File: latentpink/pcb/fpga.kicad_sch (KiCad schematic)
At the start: 0 parts

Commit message: Continued initial schematic capture and floorplanning
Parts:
- added J1: CONN_SFP_HOST, azonenberg_pcb:CONN_SFP+_AMPHENOL_UE76_A10_2000T, symbol special-azonenberg:CONN_SFP_HOST
- added J2: SFP_CAGE, azonenberg_pcb:CONN_SFP_CAGE_TE_2007194-1, symbol conn:CONN_01X01
- added U2: XC7K160T-2FBG484C, azonenberg_pcb:BGA_484_22x22_FULLARRAY_1MM, symbol xilinx-azonenberg:XC7KxT-FBG484
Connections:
- new net GND: J2.1 (P1)
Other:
- added sheet FPGA Power (fpgapwr.kicad_sch)
- added sheet QDR SRAM (qdr.kicad_sch)
- company: (none) -> Antikernel Labs

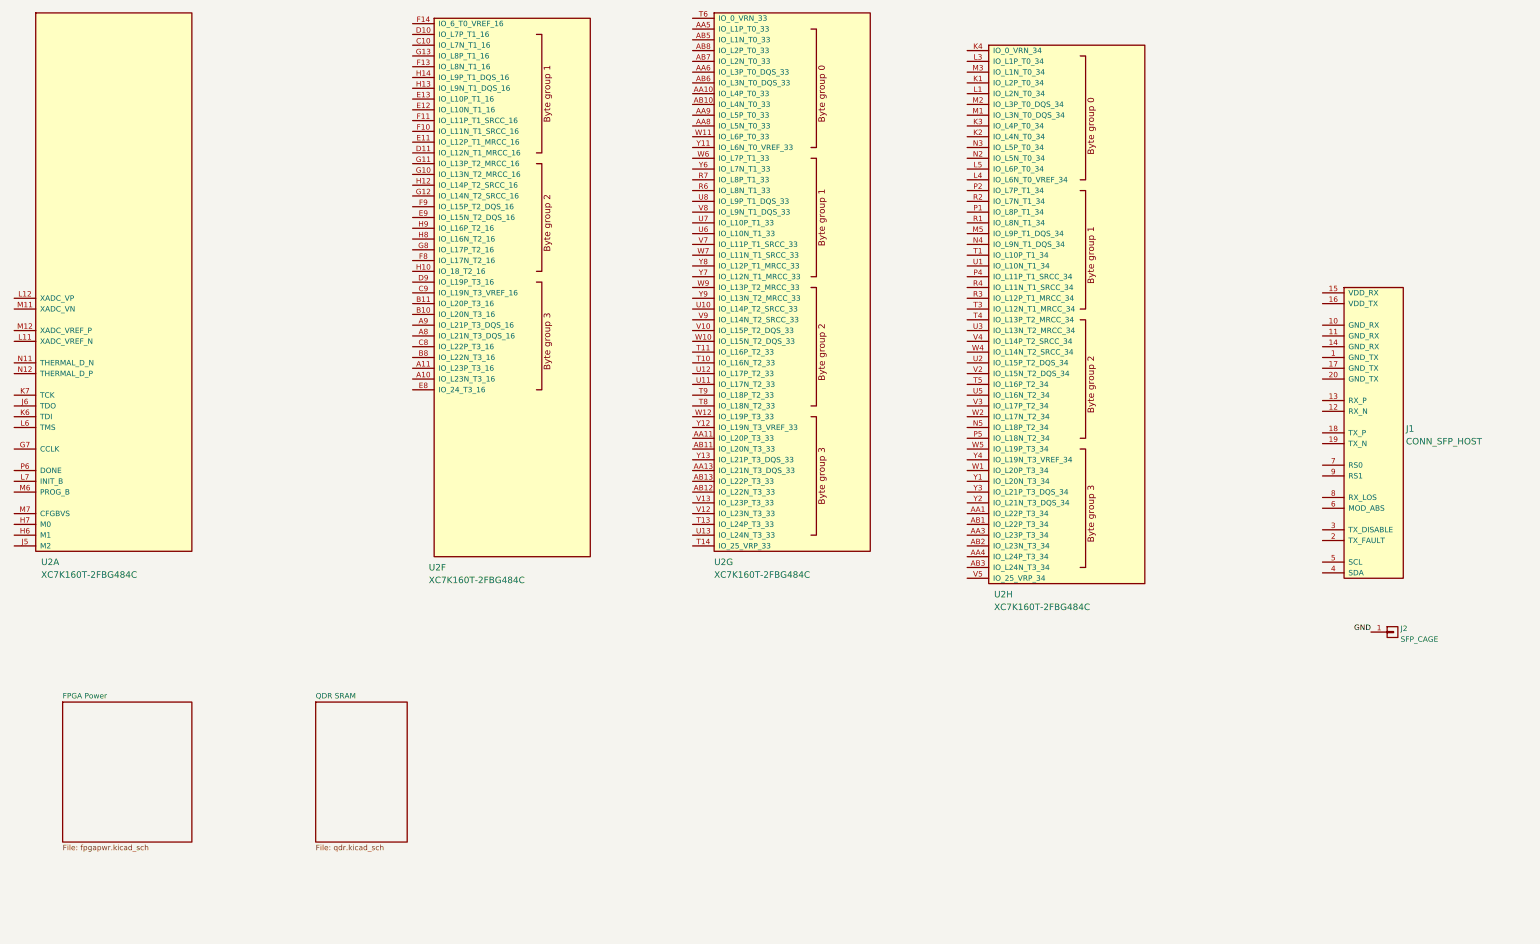
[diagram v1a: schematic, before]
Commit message: Continued initial schematic capture
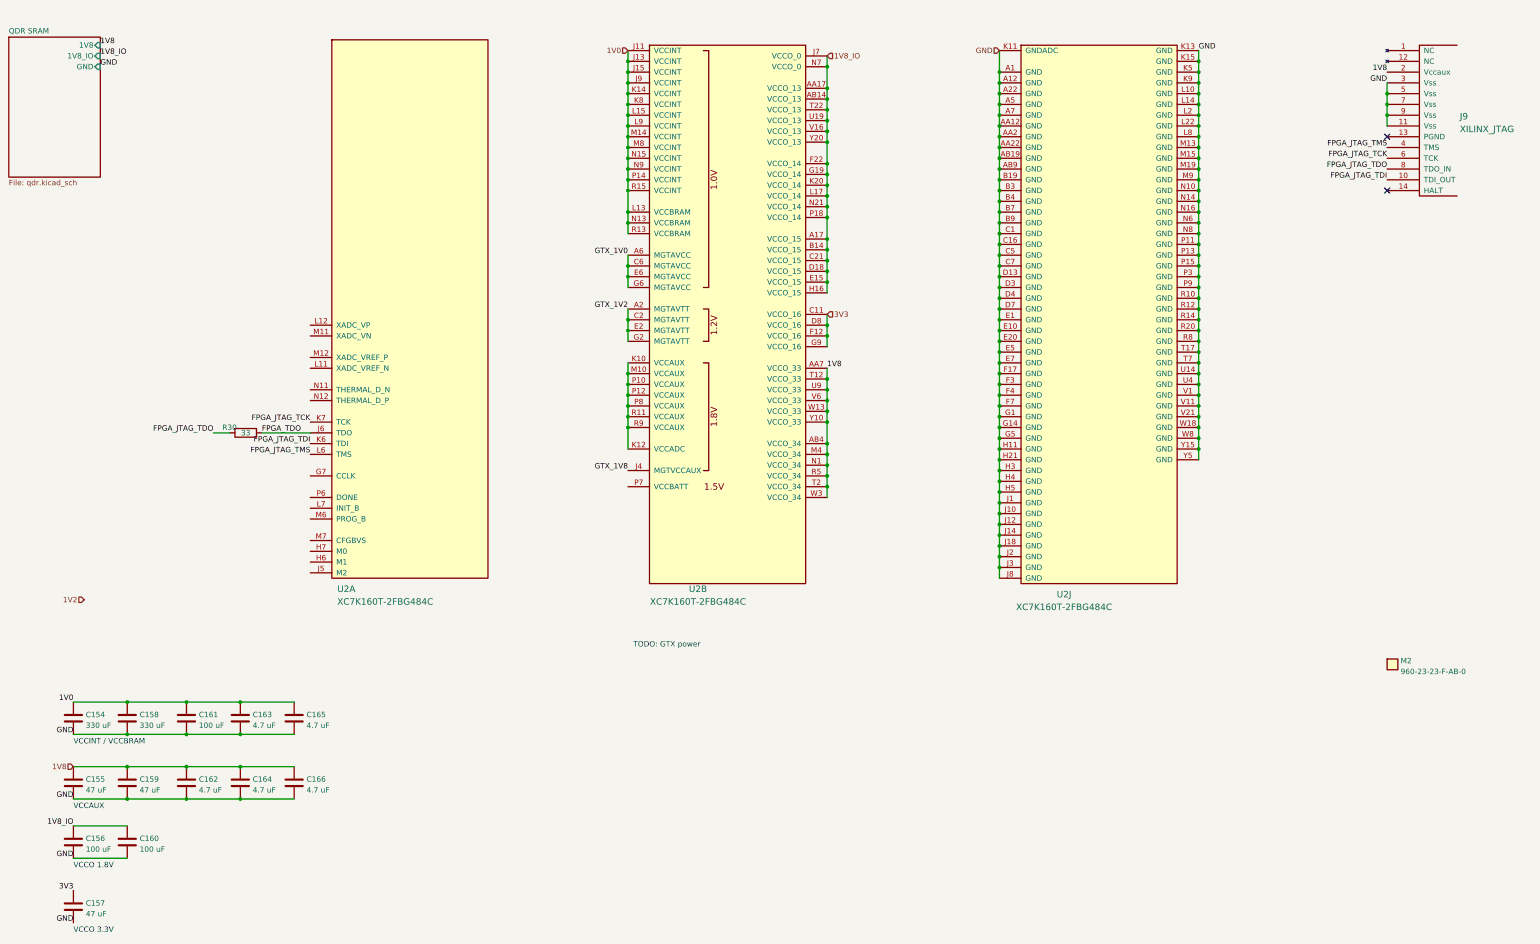
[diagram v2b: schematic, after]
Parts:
- removed J1: CONN_SFP_HOST, azonenberg_pcb:CONN_SFP+_AMPHENOL_UE76_A10_2000T, symbol special-azonenberg:CONN_SFP_HOST
- removed J2: SFP_CAGE, azonenberg_pcb:CONN_SFP_CAGE_TE_2007194-1, symbol conn:CONN_01X01
- removed unit 7 of U2
- removed unit 8 of U2
- removed unit 6 of U2
- added C154, C158: 330 uF, symbol device:C
- added C155, C157, C159: 47 uF, symbol device:C
- added C156, C160, C161: 100 uF, symbol device:C
- added C162, C163, C164, C165, C166: 4.7 uF, azonenberg_pcb:EIA_0603_CAP_NOSILK, symbol device:C
- added J9: XILINX_JTAG, azonenberg_pcb:XILINX_JTAG_PTH_MOLEX_0878311420, symbol xilinx-azonenberg:XILINX_JTAG
- added M2: 960-23-23-F-AB-0, azonenberg_pcb:HEATSINK_WAKEFIELDVETTE_960-23-23-F-AB-0, symbol special-azonenberg:MECHANICAL
- added R30: 33, azonenberg_pcb:EIA_0402_RES_NOSILK, symbol device:R
- added unit 2 of U2
- added unit 10 of U2
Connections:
- net GND: now also C154.2, C155.2, C156.2, C157.2, C158.2, C159.2, C160.2, C161.2, C162.2, C163.2, C164.2, C165.2, C166.2, J9.11 (Vss), J9.3 (Vss), J9.5 (Vss), J9.7 (Vss), J9.9 (Vss), U2.A1 (GND), U2.A12 (GND), U2.A22 (GND), U2.A5 (GND), U2.A7 (GND), U2.AA12 (GND), U2.AA2 (GND), U2.AA22 (GND), U2.AB19 (GND), U2.AB9 (GND), U2.B19 (GND), U2.B3 (GND), U2.B4 (GND), U2.B7 (GND), U2.B9 (GND), U2.C1 (GND), U2.C16 (GND), U2.C5 (GND), U2.C7 (GND), U2.D13 (GND), U2.D3 (GND), U2.D4 (GND), U2.D7 (GND), U2.E1 (GND), U2.E10 (GND), U2.E20 (GND), U2.E5 (GND), U2.E7 (GND), U2.F17 (GND), U2.F3 (GND), U2.F4 (GND), U2.F7 (GND), U2.G1 (GND), U2.G14 (GND), U2.G5 (GND), U2.H11 (GND), U2.H21 (GND), U2.H3 (GND), U2.H4 (GND), U2.H5 (GND), U2.J1 (GND), U2.J10 (GND), U2.J12 (GND), U2.J14 (GND), U2.J18 (GND), U2.J2 (GND), U2.J3 (GND), U2.J8 (GND), U2.K11 (GNDADC), U2.K13 (GND), U2.K15 (GND), U2.K5 (GND), U2.K9 (GND), U2.L10 (GND), U2.L14 (GND), U2.L2 (GND), U2.L22 (GND), U2.L8 (GND), U2.M13 (GND), U2.M15 (GND), U2.M19 (GND), U2.M9 (GND), U2.N10 (GND), U2.N14 (GND), U2.N16 (GND), U2.N6 (GND), U2.N8 (GND), U2.P11 (GND), U2.P13 (GND), U2.P15 (GND), U2.P3 (GND), U2.P9 (GND), U2.R10 (GND), U2.R12 (GND), U2.R14 (GND), U2.R20 (GND), U2.R8 (GND), U2.T17 (GND), U2.T7 (GND), U2.U14 (GND), U2.U4 (GND), U2.V1 (GND), U2.V11 (GND), U2.V21 (GND), U2.W18 (GND), U2.W8 (GND), U2.Y15 (GND), U2.Y5 (GND)
- net FPGA_TDO: now reaches U2.J6 (TDO)
- net FPGA_TDO: now also R30.1
- net FPGA_JTAG_TDI: now reaches U2.K6 (TDI)
- net FPGA_JTAG_TDI: now also J9.10 (TDI_OUT)
- net FPGA_JTAG_TCK: now reaches U2.K7 (TCK)
- net FPGA_JTAG_TCK: now also J9.6 (TCK)
- net FPGA_JTAG_TMS: now reaches U2.L6 (TMS)
- net FPGA_JTAG_TMS: now also J9.4 (TMS)
- new net: U2.K10 (VCCAUX), U2.K12 (VCCADC), U2.M10 (VCCAUX), U2.P10 (VCCAUX), U2.P12 (VCCAUX), U2.P8 (VCCAUX), U2.R11 (VCCAUX), U2.R9 (VCCAUX)
- new net 1V0: C154.1, C158.1, C161.1, C163.1, C165.1, U2.J11 (VCCINT), U2.J13 (VCCINT), U2.J15 (VCCINT), U2.J9 (VCCINT), U2.K14 (VCCINT), U2.K8 (VCCINT), U2.L13 (VCCBRAM), U2.L15 (VCCINT), U2.L9 (VCCINT), U2.M14 (VCCINT), U2.M8 (VCCINT), U2.N13 (VCCBRAM), U2.N15 (VCCINT), U2.N9 (VCCINT), U2.P14 (VCCINT), U2.R13 (VCCBRAM), U2.R15 (VCCINT)
- new net 1V8: C155.1, C159.1, C162.1, C164.1, C166.1, J9.2 (Vccaux), U2.AA7 (VCCO_33), U2.AB4 (VCCO_34), U2.M4 (VCCO_34), U2.N1 (VCCO_34), U2.R5 (VCCO_34), U2.T12 (VCCO_33), U2.T2 (VCCO_34), U2.U9 (VCCO_33), U2.V6 (VCCO_33), U2.W13 (VCCO_33), U2.W3 (VCCO_34), U2.Y10 (VCCO_33)
- new net 1V8_IO: C156.1, C160.1, U2.A17 (VCCO_15), U2.AA17 (VCCO_13), U2.AB14 (VCCO_13), U2.B14 (VCCO_15), U2.C21 (VCCO_15), U2.D18 (VCCO_15), U2.E15 (VCCO_15), U2.F22 (VCCO_14), U2.G19 (VCCO_14), U2.H16 (VCCO_15), U2.J7 (VCCO_0), U2.K20 (VCCO_14), U2.L17 (VCCO_14), U2.N21 (VCCO_14), U2.N7 (VCCO_0), U2.P18 (VCCO_14), U2.T22 (VCCO_13), U2.U19 (VCCO_13), U2.V16 (VCCO_13), U2.Y20 (VCCO_13)
- new net 3V3: C157.1, U2.C11 (VCCO_16), U2.D8 (VCCO_16), U2.F12 (VCCO_16), U2.G9 (VCCO_16)
- new net FPGA_JTAG_TDO: J9.8 (TDO_IN), R30.2
- new net GTX_1V0: U2.A6 (MGTAVCC), U2.C6 (MGTAVCC), U2.E6 (MGTAVCC), U2.G6 (MGTAVCC)
- new net GTX_1V2: U2.A2 (MGTAVTT), U2.C2 (MGTAVTT), U2.E2 (MGTAVTT), U2.G2 (MGTAVTT)
- new net GTX_1V8: U2.J4 (MGTVCCAUX)
- no-connect marks 0 -> 2
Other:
- removed sheet FPGA Power
- sheet QDR SRAM ports: added 1V8, 1V8_IO, GND; removed none
- note added: "TODO: GTX power"
- note added: "VCCAUX"
- note added: "VCCINT / VCCBRAM"
- note added: "VCCO 1.8V"
- note added: "VCCO 3.3V"
- moved on the sheet: U2A

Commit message: Continued work on schematic, mostly power supply and QDR
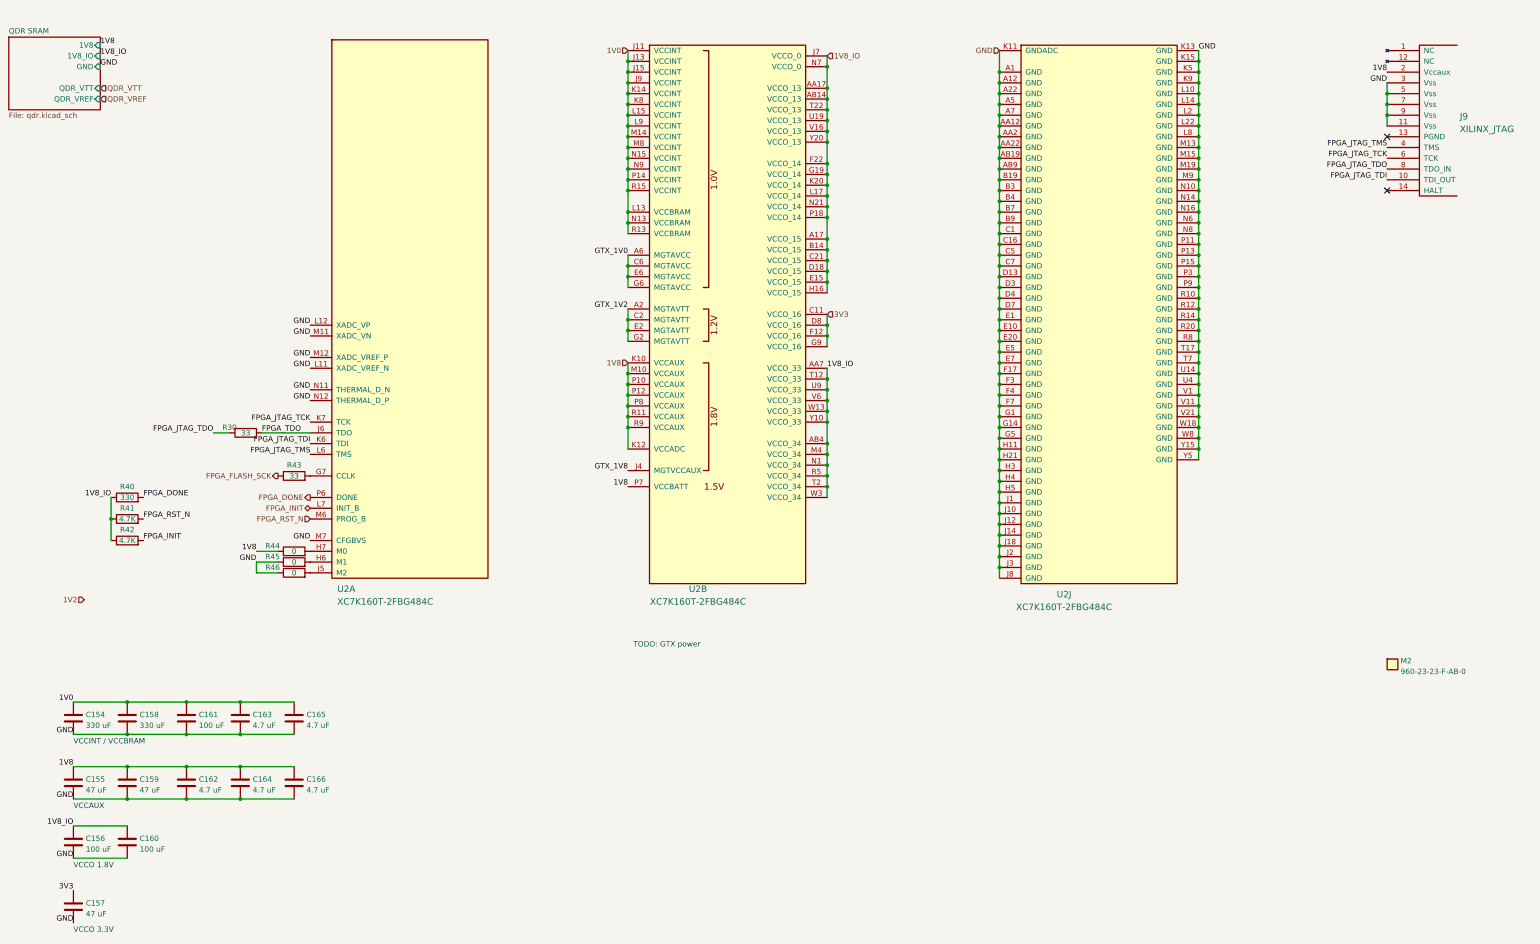
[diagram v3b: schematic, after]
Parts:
- added R40: 330, azonenberg_pcb:EIA_0402_RES_NOSILK, symbol device:R
- added R41, R42: 4.7K, azonenberg_pcb:EIA_0402_RES_NOSILK, symbol device:R
- added R43: 33, azonenberg_pcb:EIA_0402_RES_NOSILK, symbol device:R
- added R44, R45, R46: 0, azonenberg_pcb:EIA_0402_RES_NOSILK, symbol device:R
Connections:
- net 1V8: now also U2.K10 (VCCAUX), U2.K12 (VCCADC), U2.M10 (VCCAUX), U2.P10 (VCCAUX), U2.P12 (VCCAUX), U2.P7 (VCCBATT), U2.P8 (VCCAUX), U2.R11 (VCCAUX), U2.R9 (VCCAUX), R44.1; no longer U2.AA7 (VCCO_33), U2.AB4 (VCCO_34), U2.M4 (VCCO_34), U2.N1 (VCCO_34), U2.R5 (VCCO_34), U2.T12 (VCCO_33), U2.T2 (VCCO_34), U2.U9 (VCCO_33), U2.V6 (VCCO_33), U2.W13 (VCCO_33), U2.W3 (VCCO_34), U2.Y10 (VCCO_33)
- net 1V8_IO: now also U2.AA7 (VCCO_33), U2.AB4 (VCCO_34), U2.M4 (VCCO_34), U2.N1 (VCCO_34), U2.R5 (VCCO_34), U2.T12 (VCCO_33), U2.T2 (VCCO_34), U2.U9 (VCCO_33), U2.V6 (VCCO_33), U2.W13 (VCCO_33), U2.W3 (VCCO_34), U2.Y10 (VCCO_33), R40.1, R41.1, R42.1
- net GND: now also U2.L11 (XADC_VREF_N), U2.L12 (XADC_VP), U2.M11 (XADC_VN), U2.M12 (XADC_VREF_P), U2.M7 (CFGBVS), U2.N11 (THERMAL_D_N), U2.N12 (THERMAL_D_P), R45.1, R46.1
- net at U2.G7 (CCLK): now also R43.2
- net at U2.H6 (M1): now also R45.2
- net at U2.H7 (M0): now also R44.2
- net at U2.J5 (M2): now also R46.2
- net FPGA_INIT: now reaches U2.L7 (INIT_B)
- net FPGA_INIT: now also R42.2
- net FPGA_RST_N: now reaches U2.M6 (PROG_B)
- net FPGA_RST_N: now also R41.2
- net FPGA_DONE: now reaches U2.P6 (DONE)
- net FPGA_DONE: now also R40.2
- new net FPGA_FLASH_SCK: R43.1
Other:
- sheet QDR SRAM ports: added QDR_VREF, QDR_VTT; removed none

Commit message: Initial version of RGMII PHY schematic
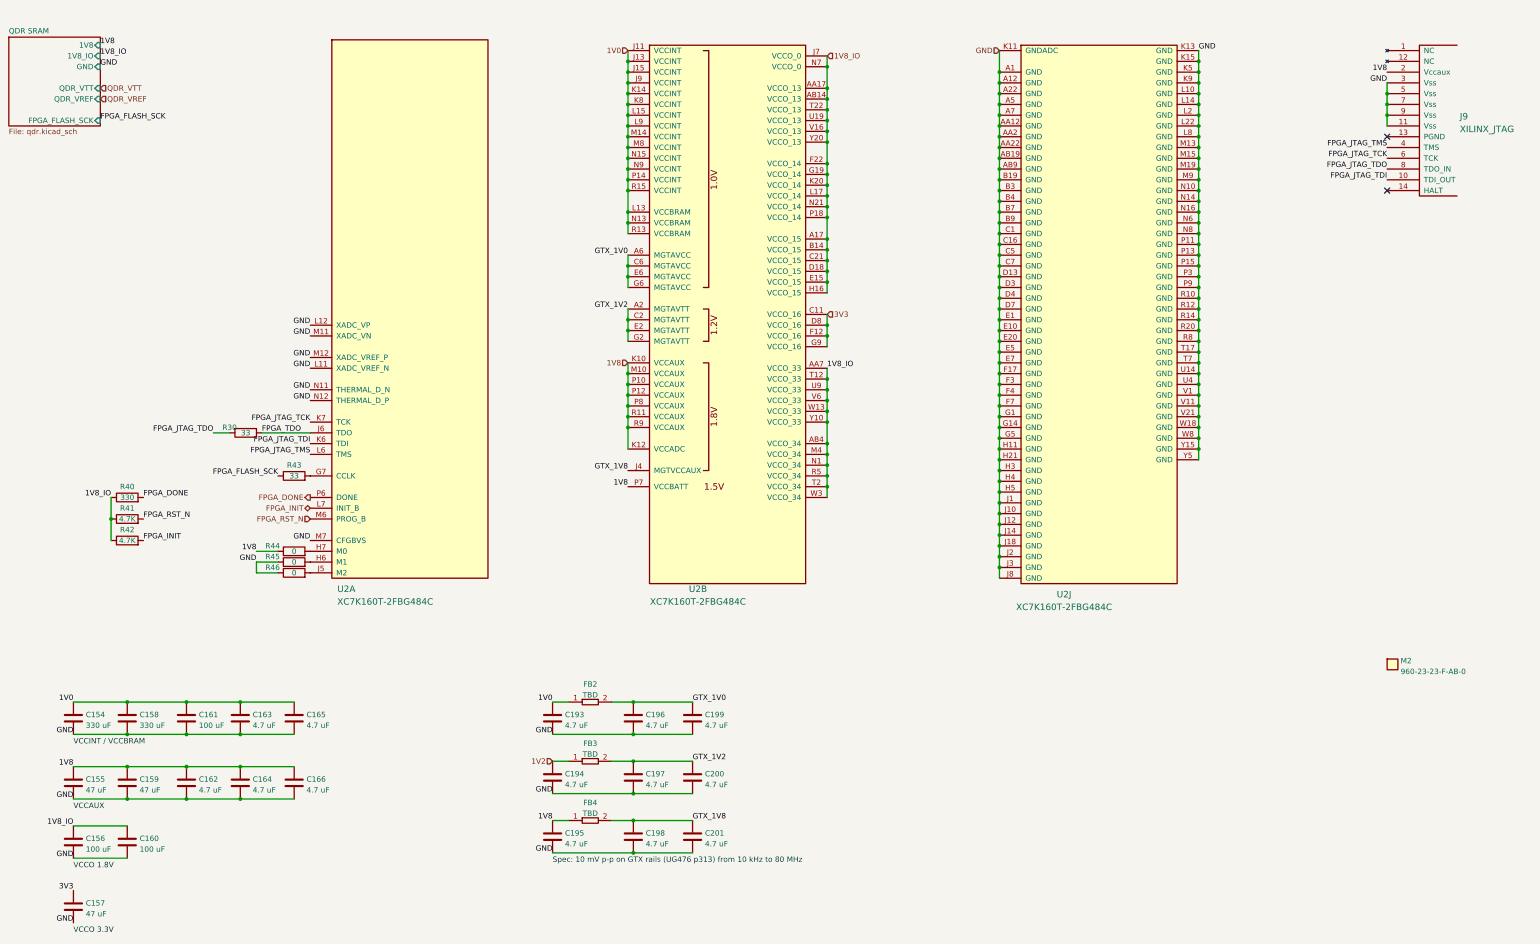
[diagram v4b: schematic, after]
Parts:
- added C193, C194, C195, C196, C197, C198, C199, C200, C201: 4.7 uF, azonenberg_pcb:EIA_0603_CAP_NOSILK, symbol device:C
- added FB2, FB3, FB4: TBD, symbol passive-azonenberg:FERRITE_SMALL2
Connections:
- net 1V0: now also C193.1, FB2.1
- net 1V2: now also C194.1, FB3.1
- net 1V8: now also C195.1, FB4.1
- net GND: now also C193.2, C194.2, C195.2, C196.2, C197.2, C198.2, C199.2, C200.2, C201.2
- net GTX_1V0: now also C196.1, C199.1, FB2.2
- net GTX_1V2: now also C197.1, C200.1, FB3.2
- net GTX_1V8: now also C198.1, C201.1, FB4.2
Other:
- sheet QDR SRAM ports: added FPGA_FLASH_SCK; removed none
- note added: "Spec: 10 mV p-p on GTX rails (UG476 p313) from 10 kHz to 80 MHz"
- note removed: "TODO: GTX power"
